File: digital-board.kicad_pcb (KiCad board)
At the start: 2 copper layers, 200 x 150 mm, 238 parts, among them IC1 ATMEGA6450-A, J1 CONN_20X2, Q1 2N3904, Q2 2N3904, SW15 TACT_SWITCH, SW16 TACT_SWITCH, SW17 TACT_SWITCH, SW18 TACT_SWITCH, SW19 TACT_SWITCH, SW20 TACT_SWITCH, SW21 TACT_SWITCH, SW22 TACT_SWITCH, SW23 TACT_SWITCH, U1 DG419, U10 74LVC1G32, U12 74AC595, U13 74AC595, U14 74HC165, U15 74AC595, U16 74AC595, U2 74HC4067, U3 R-78E5.0-1.0, U4 74HC4067, U5 74LS573, U6 74LS573, U7 74LVC2G04, U8 74AC595, U9 74HC165, X1 MIDI OUT, X2 MIDI IN, X3 MIDI THRU

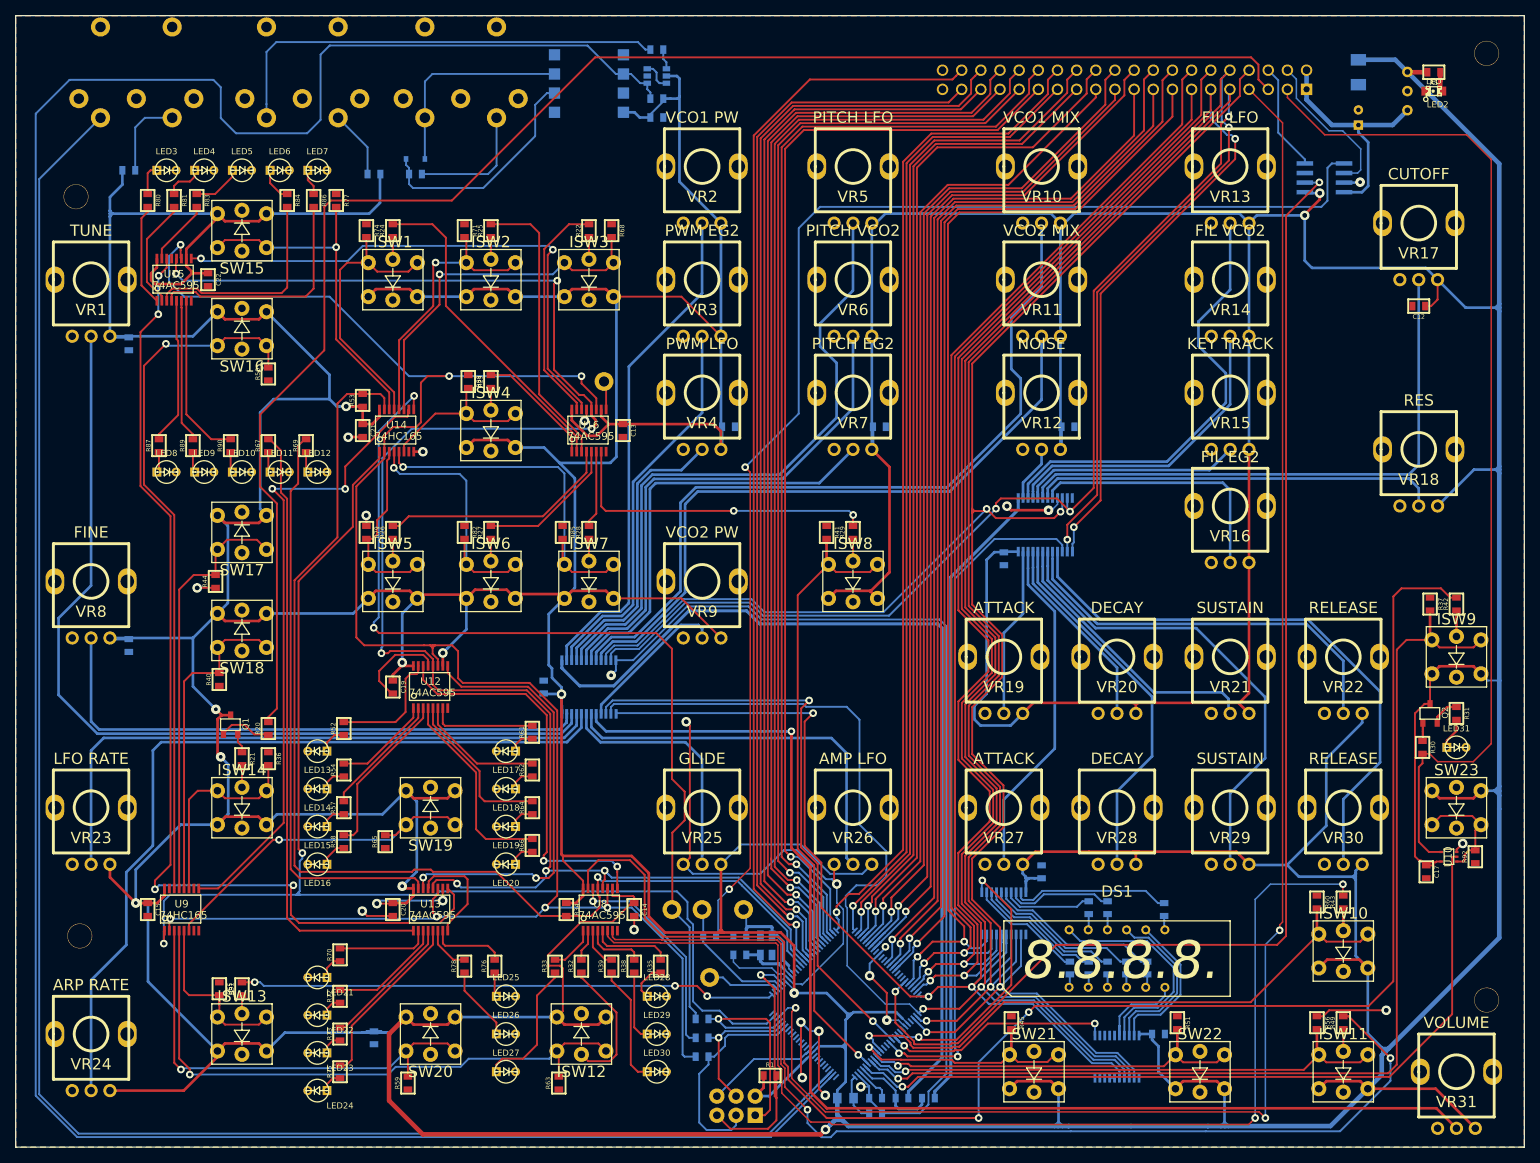
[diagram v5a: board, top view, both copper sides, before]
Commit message: silkscreen editing in 5112
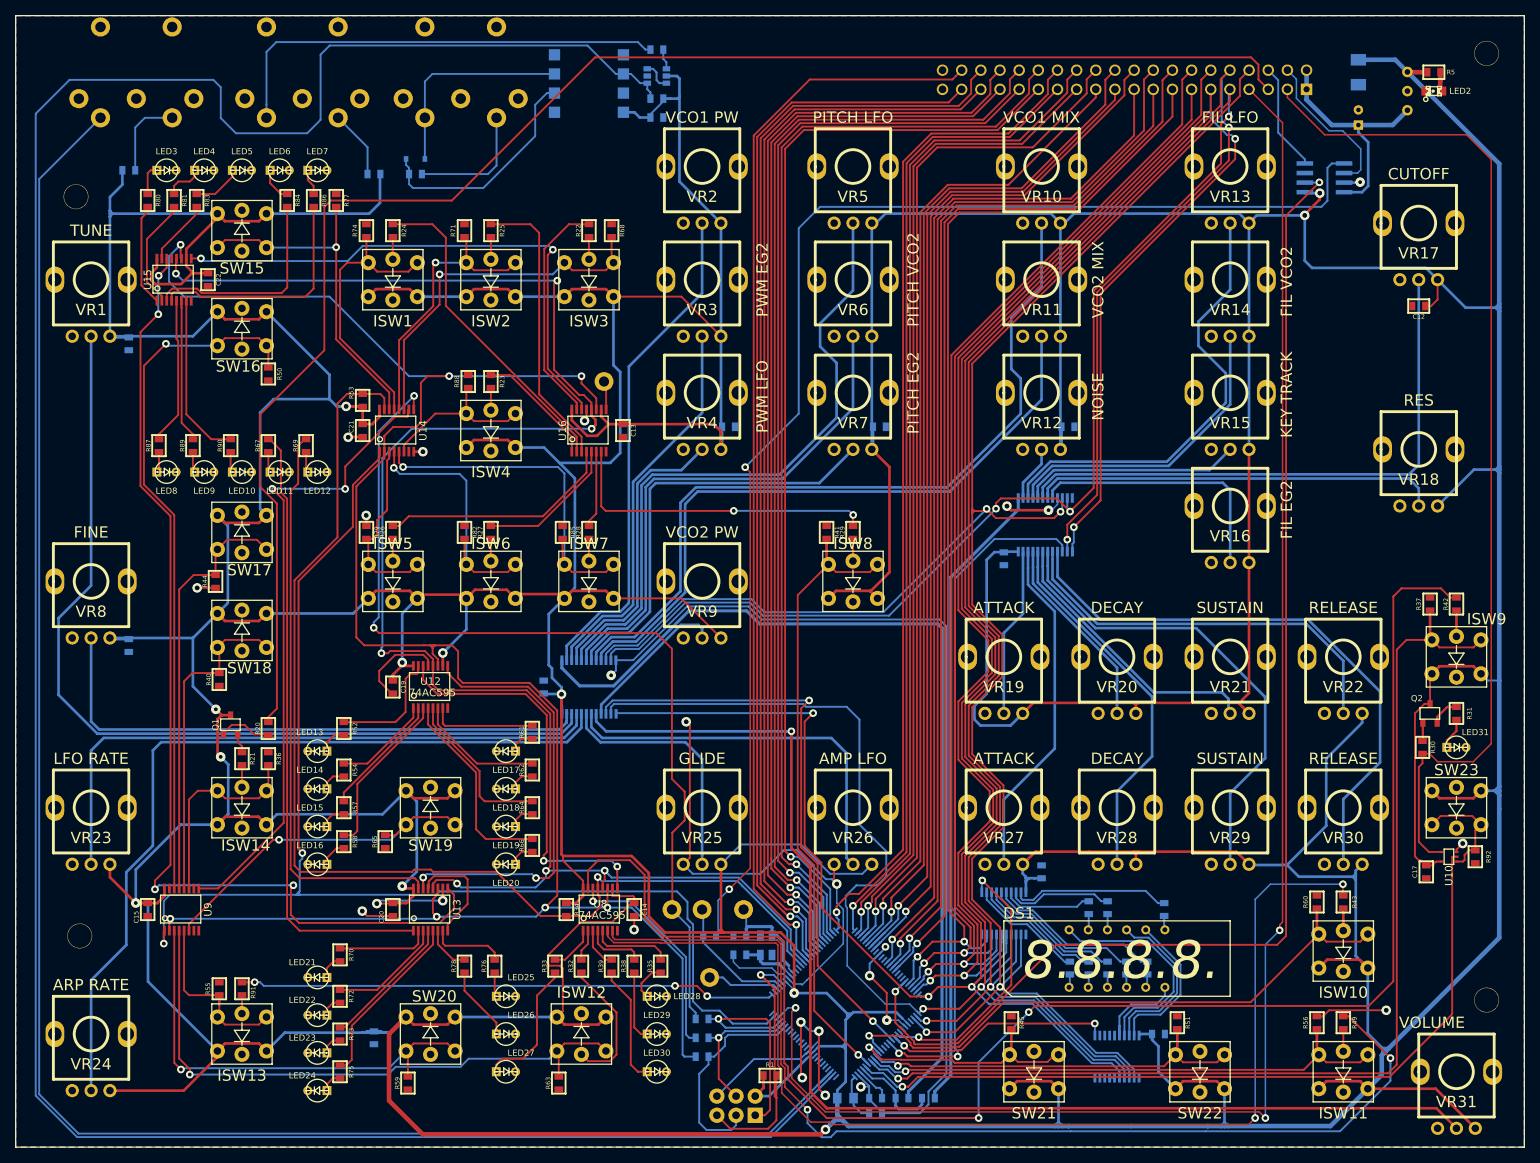
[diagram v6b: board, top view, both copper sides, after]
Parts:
- ISP1: value CONN_3X2 -> ISP
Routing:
- net +5V: track 1830.7 -> 1831.7 mm

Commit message: fixed Alpha pot footprint
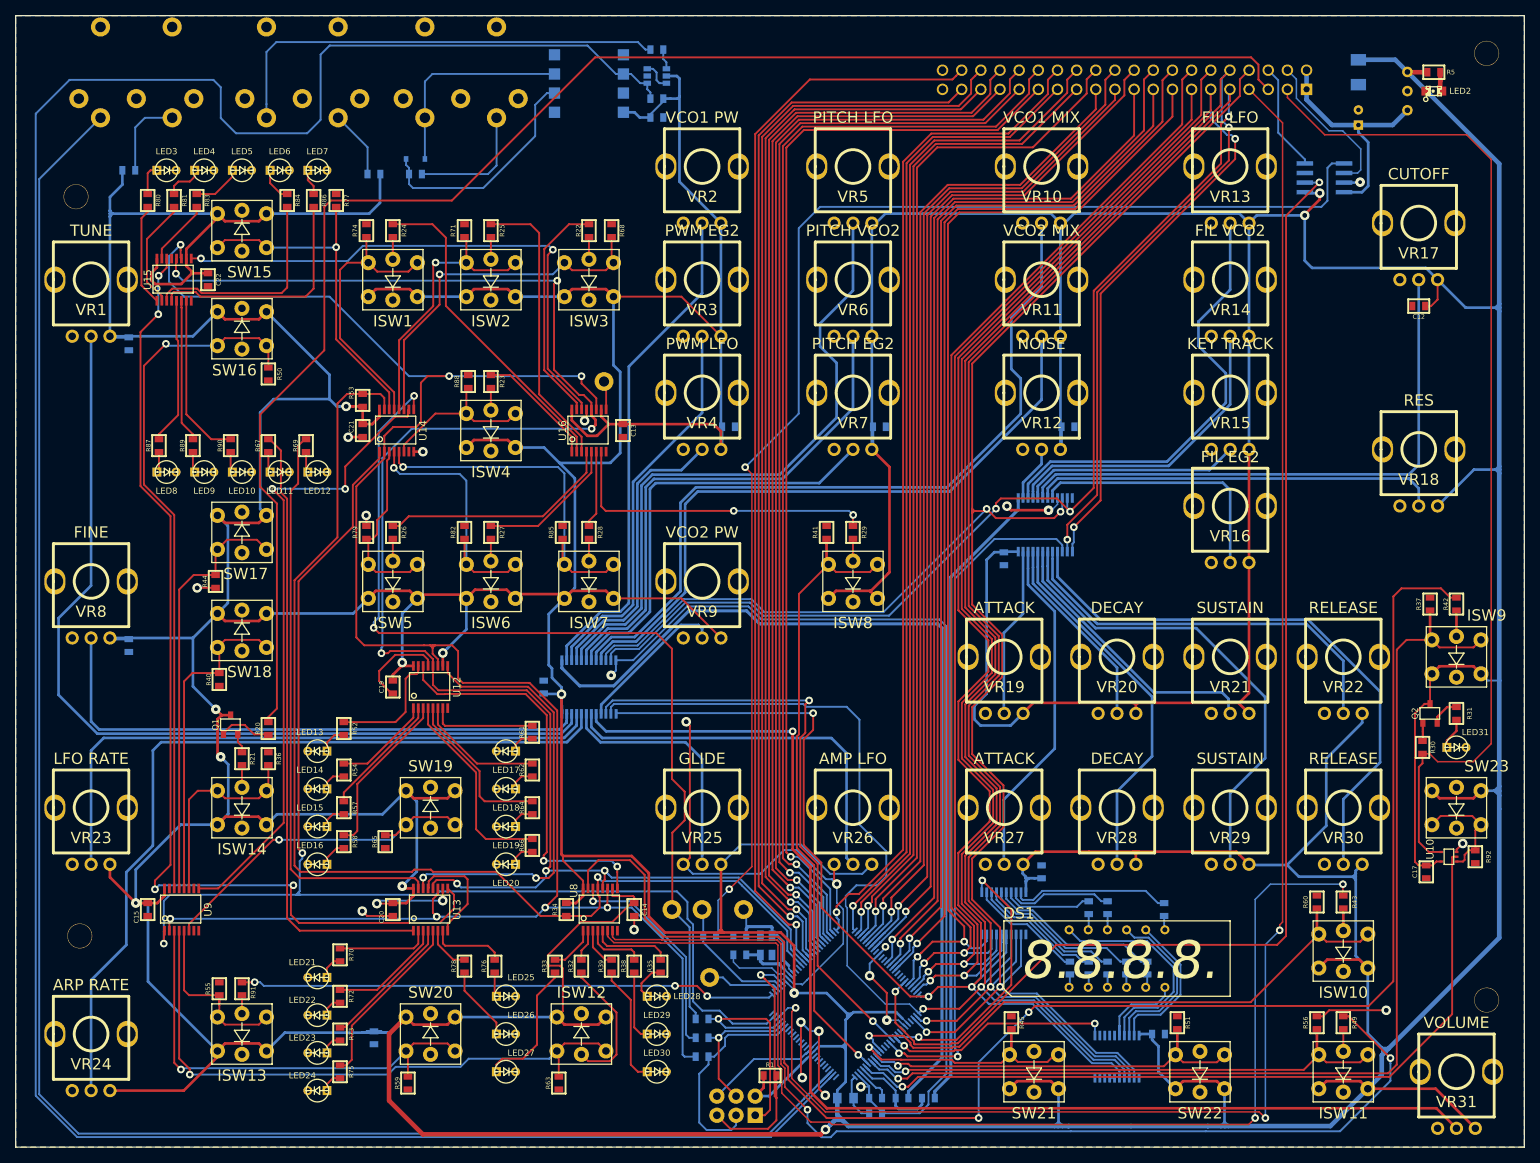
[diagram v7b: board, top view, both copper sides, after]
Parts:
- moved VR19 0.05 mm to (131.1, 85.0)
- moved VR27 0.05 mm to (131.1, 105.0)
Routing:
- net /DAC10: track 130.3 -> 131.2 mm
- net +5V: track 1831.7 -> 1831.1 mm
- net /DAC0: track 143.4 -> 142.9 mm

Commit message: updated MIDI conn footprint and 3D models
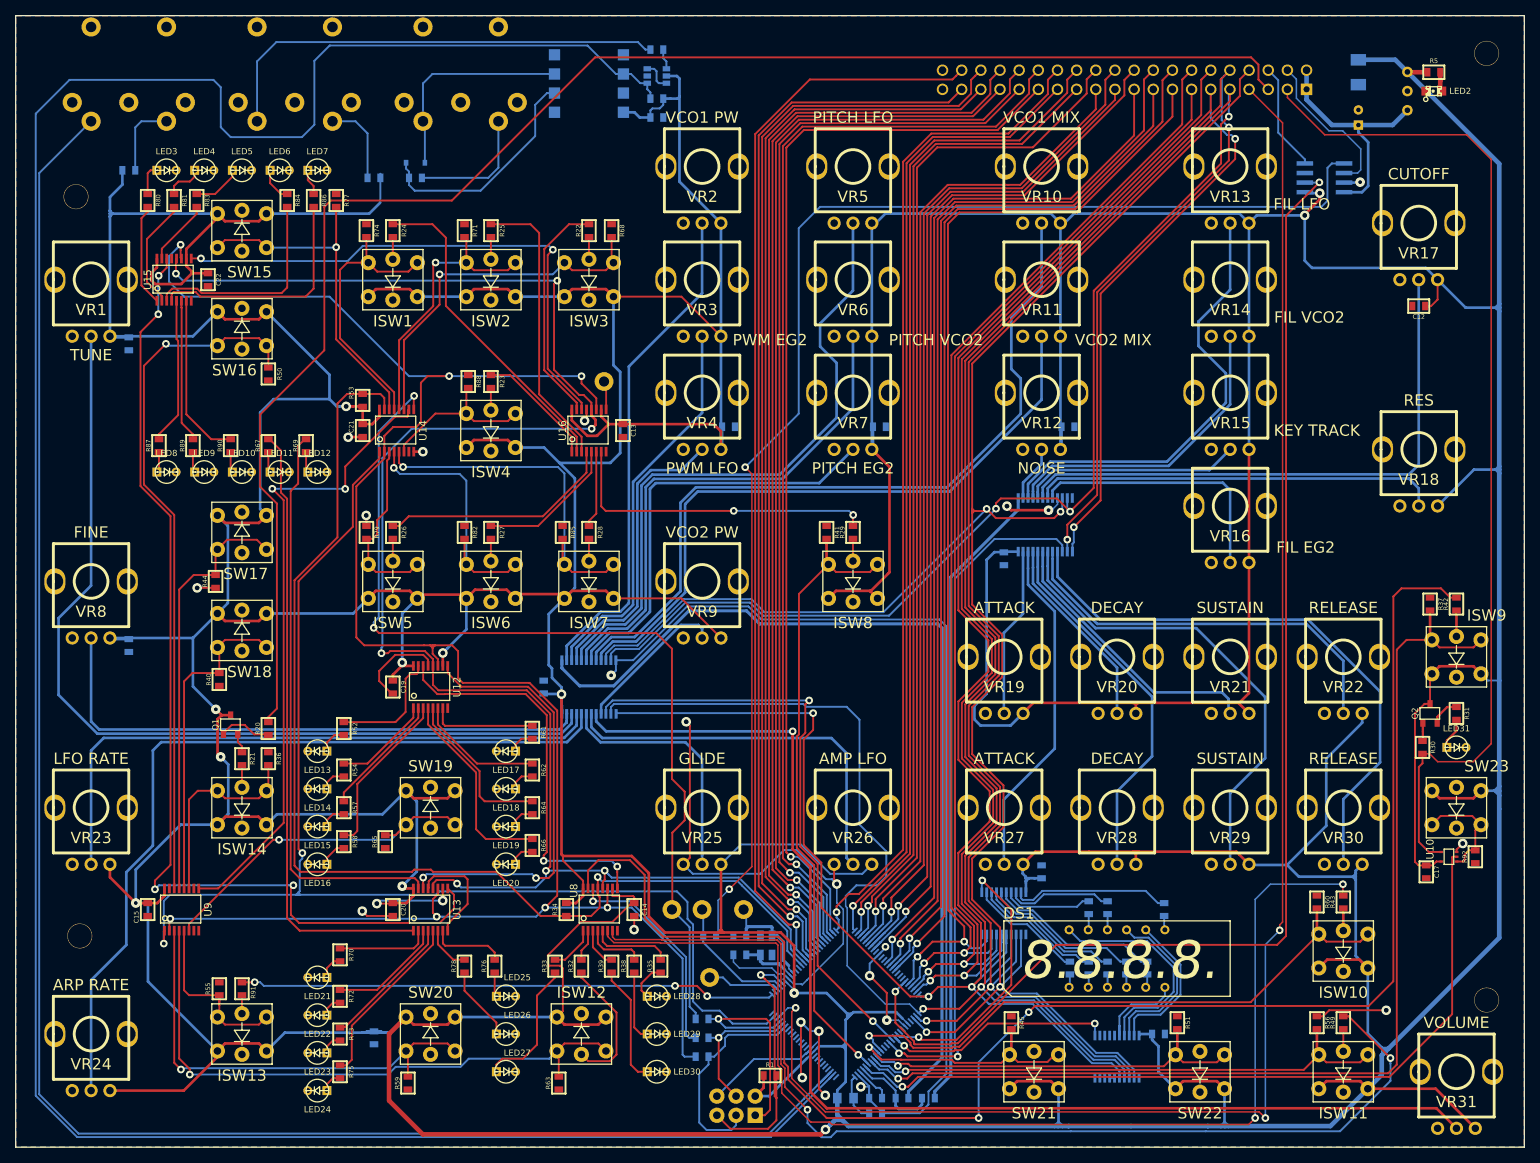
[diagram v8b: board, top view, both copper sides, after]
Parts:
- C1, C10, C11, C12, C13, C14, C15, C16, C17, C18, C19, C2, C20, C21, C22, C23, C24, C25, C26, C3, C4, C5, C7, C9: footprint synth:SM0603-JRL -> MyModules:SM0603-C-JRL
- ISP1: value ISP -> CONN_3X2
- LED2: footprint synth:LED-0805-JRL -> MyModules:LED-0805-JRL
- R1, R10, R11, R12, R13, R14, R15, R16, R17, R18, R19, R2, R20, R21, R22, R23, R24, R25, R26, R27, R28, R29, R3, R30, R31, R32, R33, R34, R35, R36, R37, R38, R39, R40, R41, R42, R43, R44, R45, R46, R47, R48, R49, R5, R50, R51, R52, R53, R54, R55, R56, R57, R58, R59, R6, R60, R61, R62, R63, R64, R65, R66, R67, R68, R69, R7, R70, R71, R72, R73, R74, R75, R76, R77, R78, R79, R8, R80, R81, R82, R83, R84, R85, R86, R87, R88, R89, R9, R90, R91, R92: footprint synth:SM0603-JRL -> MyModules:SM0603-R-JRL
- moved X1 1.12 mm to (15.0, 11.5)
- moved X3 1.12 mm to (37.0, 11.5)
- moved D1 0.50 mm to (53.0, 19.5)
- moved R19 0.50 mm to (47.5, 21.5)
- moved R7 0.50 mm to (53.0, 21.5)
- moved X2 0.50 mm to (59.0, 11.5)
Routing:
- net Net-(R19-Pad2): track 9.08 -> 11.2 mm
- net UART RX: track 344.5 -> 345.5 mm
- net UART TX: track 245.8 -> 244.8 mm
- net Net-(R13-Pad1): track 60.6 -> 61.6 mm
- net Net-(R8-Pad2): track 11.1 -> 10.2 mm
- net Net-(D1-Pad1): track 27.9 -> 28.6 mm
